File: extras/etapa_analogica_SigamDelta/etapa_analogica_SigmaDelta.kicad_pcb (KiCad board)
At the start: 2 copper layers, 63.5 x 78.8 mm, 19 parts, among them P1 CONN_02X10, P2 CONN_01X03, P3 CONN_02X10, P4 BNC

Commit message: chasis bnc
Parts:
- added FB1: FILTER, Capacitors_SMD:C_0805_HandSoldering, F.Cu at (123.8, 76.9)
- P4: footprint Sockets_BNC:BNC_Socket_TYCO-AMP_LargePads -> chasis_bnc:chasis_bnc
- moved R6 18.6 mm to (136.1, 74.7), turned to 180 degrees
- moved P4 18.1 mm to (154.2, 58.4), turned to 0 degrees
- moved R5 15.3 mm to (131.0, 74.5)
- moved C4 12.0 mm to (137.5, 78.4)
- moved R1 7.70 mm to (128.5, 70.5), turned to 90 degrees
- moved R2 2.82 mm to (149.2, 75.7), turned to 90 degrees
- moved RV2 2.67 mm to (118.2, 82.4)
- moved R4 1.88 mm to (126.2, 76.8), turned to 270 degrees
- moved C6 1.08 mm to (134.6, 80.1)
- moved D1 1.02 mm to (120.3, 69.6)
- moved C3 0.39 mm to (130.0, 79.5)
- moved RV1 0.36 mm to (115.3, 71.7)
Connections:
- D1 pad 1: Net-(D1-Pad1) -> GND
- D1 pad 2: GND -> Net-(D1-Pad2)
- D1 pad 3: (no net) -> Net-(D1-Pad3)
- P1 pad 10: /Tx -> Net-(P1-Pad10)
- P1 pad 12: Net-(P1-Pad12) -> /Tx
- P1 pad 14: Net-(P1-Pad14) -> /Rx
- P1 pad 8: /Rx -> Net-(P1-Pad8)
- R1 pad 1: Net-(D1-Pad1) -> Net-(D1-Pad2)
- RV1 pad 1: Net-(D1-Pad1) -> Net-(D1-Pad2)

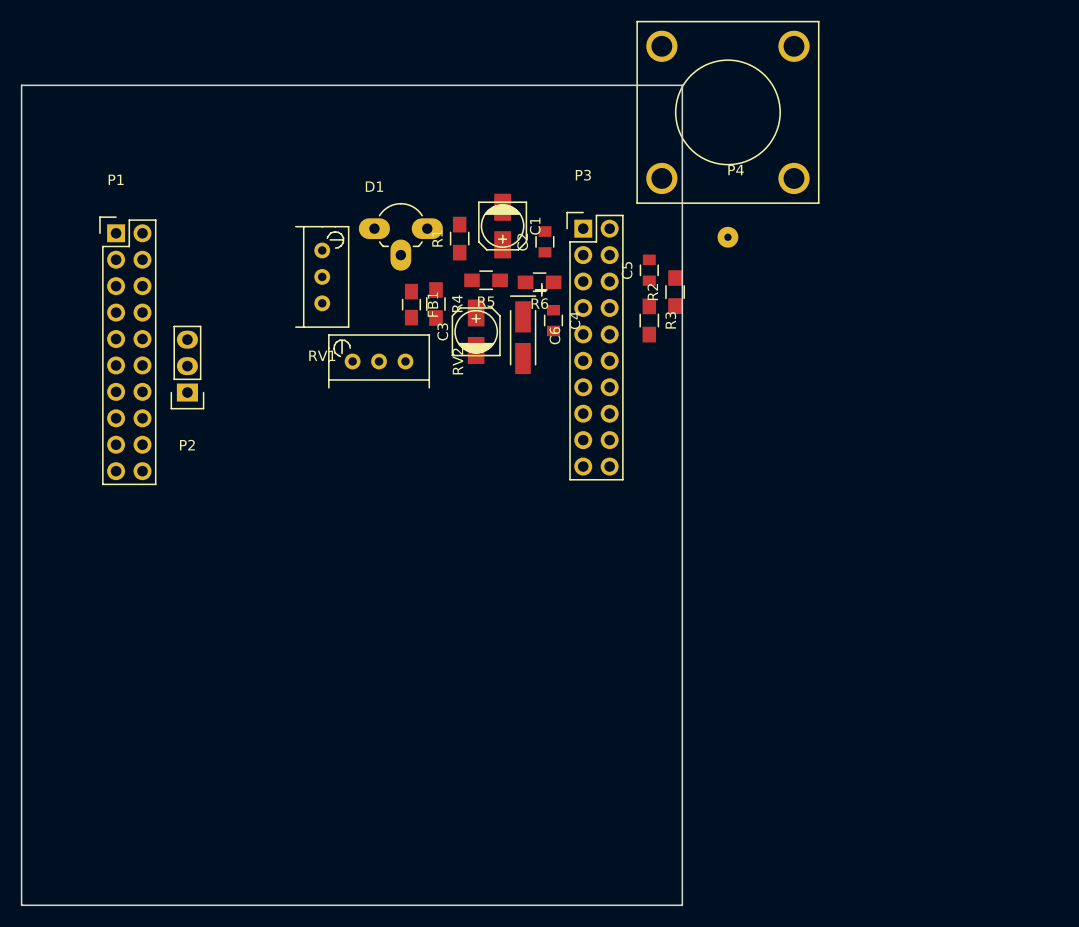
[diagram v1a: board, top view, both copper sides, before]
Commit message: Agregado rooteo placa en Kicad
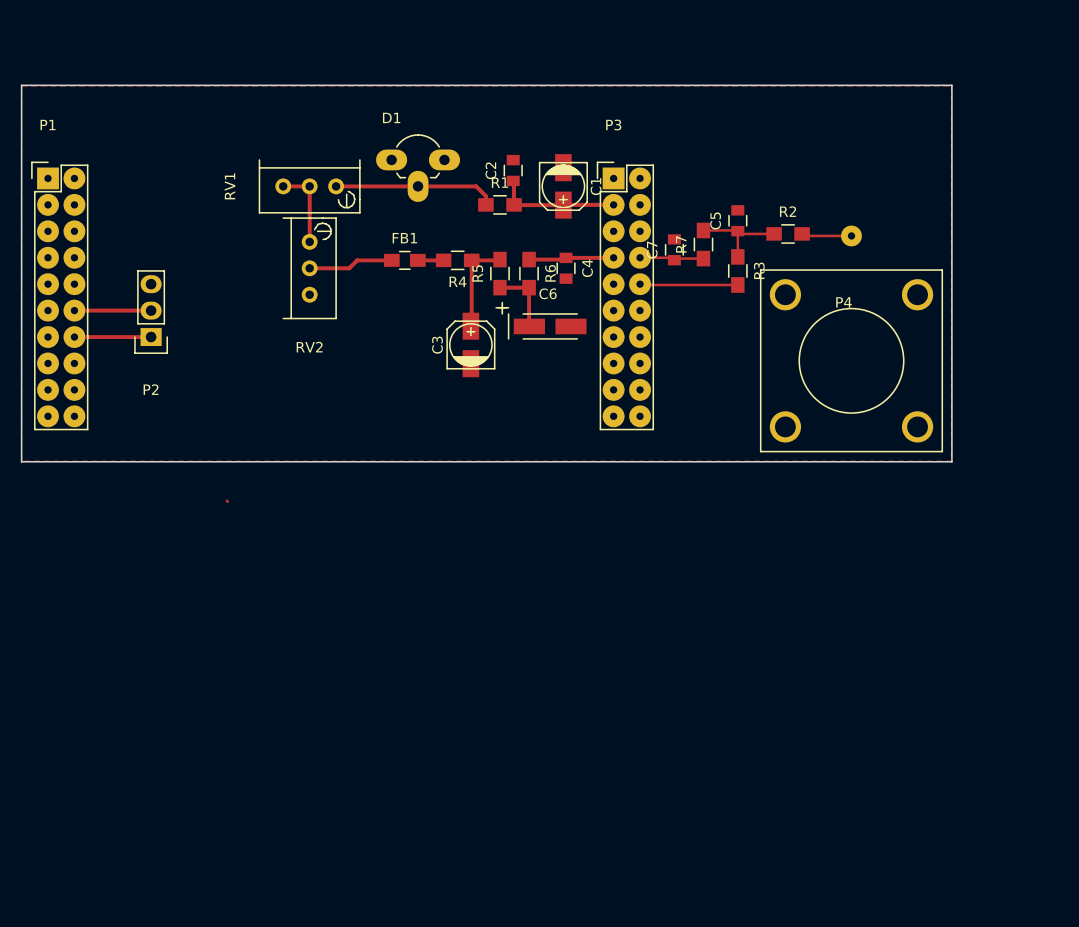
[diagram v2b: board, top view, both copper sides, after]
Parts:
- added C7: .1n, Capacitors_SMD:C_0805, F.Cu at (149.1, 71.6)
- added R7: 150k, Resistors_SMD:R_0805_HandSoldering, F.Cu at (151.9, 71.1)
- C3: value 22u -> 10u
- C4: value 1u -> 10u
- C5: value 1n -> .1n
- R2, R3: value 6,8K -> 150k
- R4: value 7,5k -> 15k
- R5, R6: value 1k -> 15k
- moved P4 26.7 mm to (166.1, 82.3), turned to 180 degrees
- moved RV2 12.2 mm to (114.0, 70.9), turned to 180 degrees
- moved R2 12.2 mm to (160.0, 70.1), turned to 0 degrees
- moved C5 9.75 mm to (155.2, 68.8)
- moved R3 9.75 mm to (155.2, 73.7)
- moved P1 8.40 mm to (88.9, 64.8)
- moved C2 7.50 mm to (133.6, 64.0)
- moved C1 6.97 mm to (138.4, 65.5)
- moved D1 6.81 mm to (121.9, 63.0)
- moved P2 6.38 mm to (98.8, 80.0)
- moved RV1 6.30 mm to (116.6, 65.5), turned to 90 degrees
- moved P3 5.64 mm to (143.3, 64.8)
- moved C4 5.16 mm to (138.7, 73.4)
- moved R1 5.05 mm to (132.3, 67.3), turned to 0 degrees
- moved R4 4.69 mm to (128.3, 72.6), turned to 180 degrees
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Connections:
- C5 pad 1: /P41 -> Net-(C5-Pad1)
- D1 pad 3: Net-(D1-Pad3) -> (no net)
- P1 pad 10: Net-(P1-Pad10) -> (no net)
- P1 pad 11: Net-(P1-Pad11) -> (no net)
- P1 pad 13: Net-(P1-Pad13) -> (no net)
- P1 pad 15: Net-(P1-Pad15) -> (no net)
- P1 pad 16: Net-(P1-Pad16) -> (no net)
- P1 pad 17: Net-(P1-Pad17) -> (no net)
- P1 pad 18: Net-(P1-Pad18) -> (no net)
- P1 pad 19: Net-(P1-Pad19) -> (no net)
- P1 pad 20: Net-(P1-Pad20) -> (no net)
- P1 pad 3: /3.3v -> /3,3v
- P1 pad 5: Net-(P1-Pad5) -> (no net)
- P1 pad 6: Net-(P1-Pad6) -> (no net)
- P1 pad 7: Net-(P1-Pad7) -> (no net)
- P1 pad 8: Net-(P1-Pad8) -> (no net)
- P1 pad 9: Net-(P1-Pad9) -> (no net)
- P3 pad 11: /N32 -> (no net)
- P3 pad 12: /P33 -> (no net)
- P3 pad 13: /N29 -> (no net)
- P3 pad 14: /P30 -> (no net)
- P3 pad 15: /N26 -> (no net)
- P3 pad 16: /P27 -> (no net)
- P3 pad 17: /N23 -> (no net)
- P3 pad 18: /P24 -> (no net)
- P3 pad 19: /N21 -> (no net)
- P3 pad 20: /P22 -> (no net)
- P3 pad 3: /3.3v -> /3,3v
- P3 pad 5: /N50 -> (no net)
- P3 pad 6: /P51 -> (no net)
- P3 pad 9: /N34 -> (no net)
- R2 pad 1: /P41 -> Net-(C5-Pad1)
- R3 pad 1: /P41 -> Net-(C5-Pad1)
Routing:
- net Net-(D1-Pad2): track 0.00 -> 15.9 mm
- net /3,3v: track 0.00 -> 11.9 mm
- net /P35: track 0.00 -> 9.54 mm
- net Net-(C5-Pad1): track 0.00 -> 9.39 mm
- net Net-(C3-Pad1): track 0.00 -> 9.11 mm
- net Net-(FB1-Pad1): track 0.00 -> 8.21 mm
- net /N40: track 0.00 -> 8.20 mm
- net Net-(RV1-Pad2): track 0.00 -> 7.87 mm
- net /Tx: track 0.00 -> 7.37 mm
- net /Rx: track 0.00 -> 7.37 mm
- net Net-(C6-Pad1): track 0.00 -> 6.54 mm
- net /P41: track 0.00 -> 6.26 mm
- net Net-(P4-Pad1): track 0.00 -> 4.83 mm
- net Net-(FB1-Pad2): track 0.00 -> 2.48 mm
- added copper zone on F.Cu, net GND
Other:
- board size 63.5 x 78.8 mm -> 89.4 x 36.2 mm
